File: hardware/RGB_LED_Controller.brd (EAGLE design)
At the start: 60 x 37 mm, 17 parts, among them IC2 MEGA8-AI, J2 CON_HEADER_1X04, Q1 MOSFET-NCHANNELFDD8580, Q2 MOSFET-NCHANNELFDD8580, Q4 MOSFET-NCHANNELFDD8580

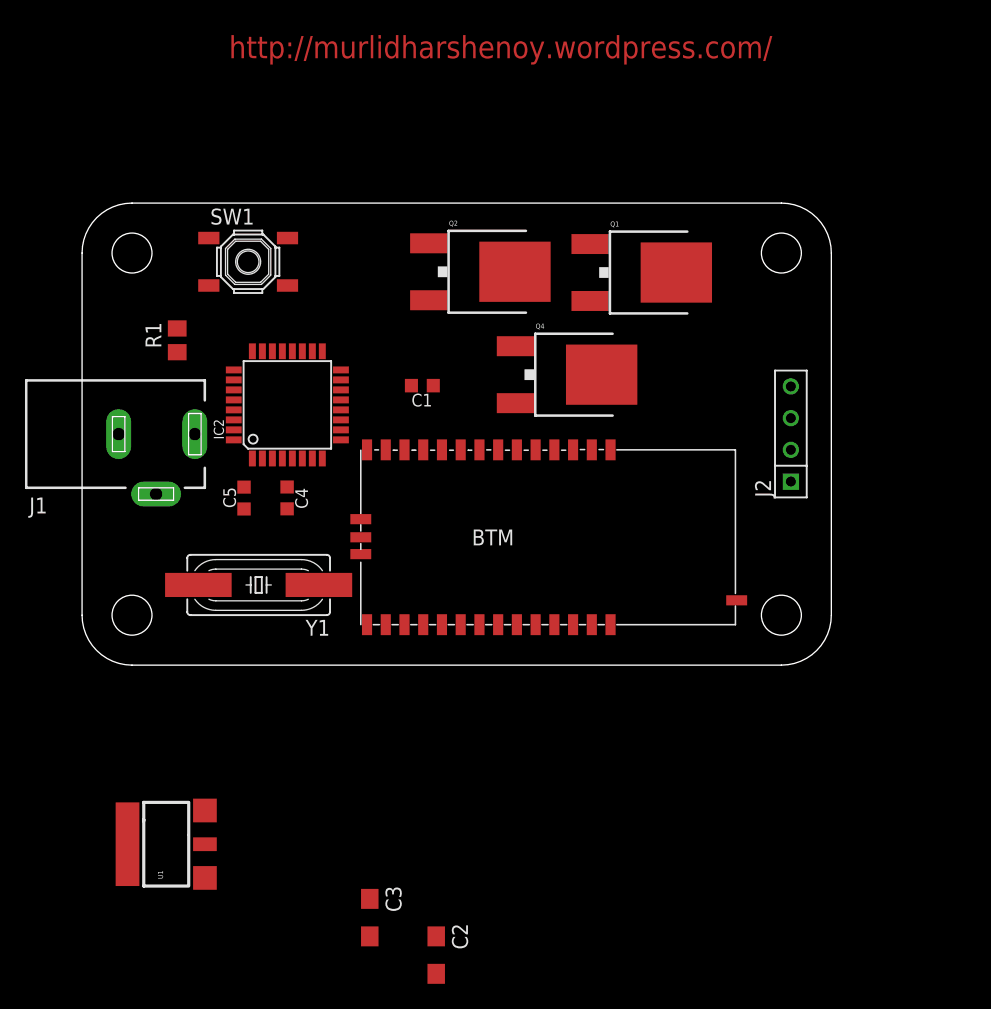
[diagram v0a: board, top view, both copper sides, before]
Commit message: some routing done. PCB modified to 7043
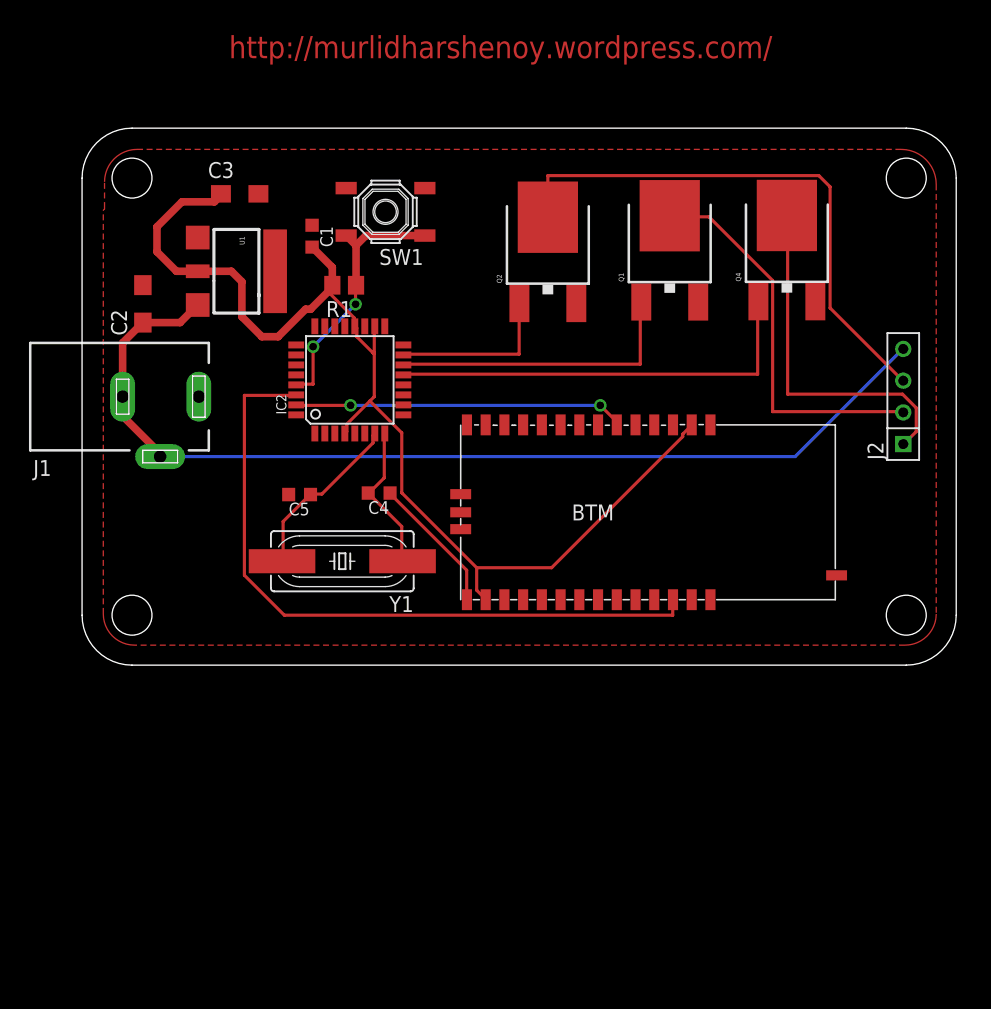
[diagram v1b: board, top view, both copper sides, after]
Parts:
- removed U$3: (no value), dp_devices:DP6037_V1
- added U$1: (no value), dp_devices:DP7043_V1
- moved C3 58.9 mm to (12.6, 37.7), turned to 0 degrees
- moved C2 57.2 mm to (4.87, 28.9), turned to 90 degrees
- moved U1 46.2 mm to (12.4, 31.5), turned to 270 degrees
- moved Q4 19.9 mm to (56.4, 34.4), turned to 0 degrees
- moved C1 14.9 mm to (18.4, 34.4), turned to 270 degrees
- moved R1 14.1 mm to (21.0, 30.4), turned to 180 degrees
- moved SW1 11.7 mm to (24.3, 36.3), turned to 180 degrees
- moved J2 9.49 mm to (65.8, 17.7)
- moved U$4 8.25 mm to (30.3, 5.24)
- moved C4 7.38 mm to (23.8, 13.8), turned to 180 degrees
- moved Y1 6.96 mm to (20.8, 8.32)
- moved IC2 5.39 mm to (21.4, 22.8)
- moved Q2 5.05 mm to (37.3, 34.3), turned to 0 degrees
- moved C5 4.46 mm to (17.4, 13.7), turned to 180 degrees
- moved Q1 3.14 mm to (47.1, 34.4), turned to 0 degrees
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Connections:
- net GND: now also U$4.PIO5
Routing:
- net +3V3: track 0.00 -> 91.0 mm
- net 12V: track 0.00 -> 80.8 mm
- net TX: track 0.00 -> 55.4 mm
- net N$8: track 0.00 -> 44.3 mm
- net N$1: track 0.00 -> 34.3 mm
- net N$7: track 0.00 -> 31.4 mm
- net N$6: track 0.00 -> 28.5 mm
- net RX: track 0.00 -> 26.5 mm, vias 0 -> 2
- net N$2: track 0.00 -> 24.0 mm
- net N$4: track 0.00 -> 20.9 mm, vias 0 -> 2
- net N$5: track 0.00 -> 13.8 mm
- net N$3: track 0.00 -> 13.4 mm
- net N$9: track 0.00 -> 11.9 mm
- net GND: track 0.00 -> 11.2 mm
- added copper zone on layer 1, net GND
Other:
- board size 60 x 37 mm -> 70 x 43 mm

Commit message: routing done.Optimize before printing
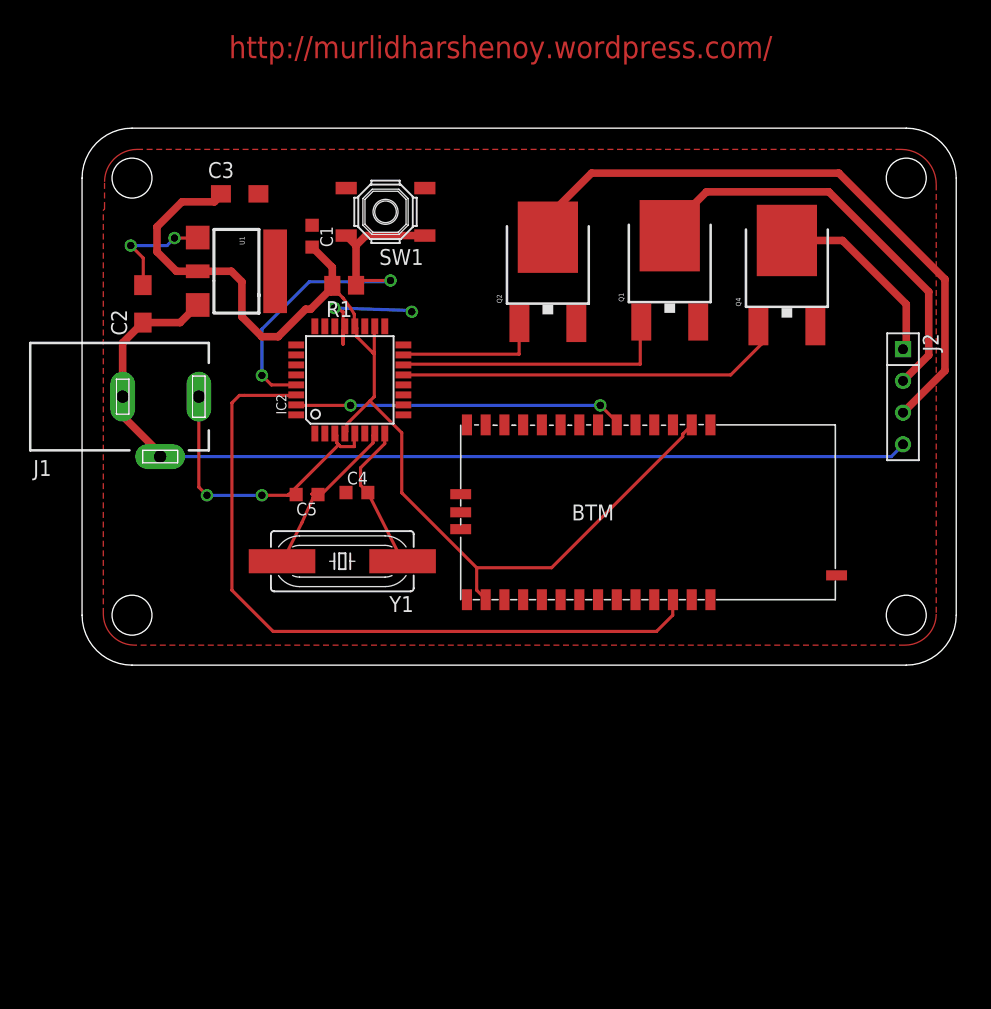
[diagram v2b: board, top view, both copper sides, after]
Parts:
- moved J2 7.60 mm to (65.7, 25.3), turned to 270 degrees
- moved Q4 2.00 mm to (56.4, 32.4)
- moved C4 1.78 mm to (22.0, 13.8), turned to 0 degrees
- moved Q1 1.60 mm to (47.1, 32.8)
- moved Q2 1.60 mm to (37.3, 32.7)
- moved C5 0.60 mm to (18.0, 13.7)
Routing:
- net GND: track 11.2 -> 46.6 mm, vias 0 -> 6
- net N$6: track 28.5 -> 15.4 mm
- net N$4: track 20.9 -> 31.7 mm
- net N$8: track 44.3 -> 50.5 mm
- net TX: track 55.4 -> 58.9 mm
- net 12V: track 80.8 -> 77.7 mm
- net N$1: track 34.3 -> 31.2 mm
- net N$7: track 31.4 -> 33.8 mm
- net N$2: track 24.0 -> 22.4 mm
- net N$3: track 13.4 -> 11.8 mm

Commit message: PCB labelled
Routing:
- net 12V: track 77.7 -> 82.4 mm
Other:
- board text added: "11.2012"
- board text added: "BT LED CNTRLR V2"
- board text added: "MURALIDHAR S."
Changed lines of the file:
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@@
 <?xml version="1.0" encoding="utf-8"?>
 <!DOCTYPE eagle SYSTEM "eagle.dtd">
-<eagle version="6.2">
+<eagle version="6.1">
 <drawing>
 <settings>
@@
 <board>
 <plain>
-<text x="11.76" y="48.6" size="1.778" layer="1">http://murlidharshenoy.wordpress.com/</text>
+<text x="7.66" y="40.7" size="1.778" layer="27">http://murlidharshenoy.wordpress.com/</text>
 <polygon width="0.4064" layer="41">
 <vertex x="52.2" y="19.4"/>
@@
 <vertex x="51.5" y="19.4"/>
 </polygon>
+<text x="62.1" y="26.7" size="1.778" layer="1" rot="R270">MURALIDHAR S.</text>
+<text x="8.6" y="39.3" size="1.27" layer="1">BT LED CNTRLR V2</text>
+<text x="66.9" y="18.2" size="1.778" layer="1" rot="R270">11.2012</text>
 </plain>
 <attributes>
@@
 <wire x1="6.3" y1="16.7" x2="6.4" y2="16.8" width="0.254" layer="1"/>
 <wire x1="6.3" y1="16.7" x2="6.25" y2="16.7" width="0.254" layer="1"/>
-<wire x1="64.8" y1="16.7" x2="65.7" y2="17.6" width="0.254" layer="16"/>
-<wire x1="6.3" y1="16.7" x2="64.8" y2="16.7" width="0.254" layer="16"/>
+<wire x1="64.7" y1="17.6" x2="65.7" y2="17.6" width="0.8128" layer="16"/>
 <wire x1="65.7" y1="17.6" x2="65.74" y2="17.68" width="0.254" layer="16"/>
 <wire x1="6.3" y1="16.7" x2="6.25" y2="16.7" width="0.254" layer="16"/>
+<wire x1="6.3" y1="16.7" x2="30.9" y2="16.7" width="0.8128" layer="16"/>
+<wire x1="30.9" y1="16.7" x2="30.9" y2="19.4" width="0.8128" layer="16"/>
+<wire x1="30.9" y1="19.4" x2="43.1" y2="19.4" width="0.8128" layer="16"/>
+<wire x1="43.1" y1="19.4" x2="43.1" y2="20.7" width="0.8128" layer="16"/>
+<wire x1="43.1" y1="20.7" x2="60.8" y2="20.7" width="0.8128" layer="16"/>
+<wire x1="60.8" y1="20.7" x2="64.7" y2="17.6" width="0.8128" layer="16"/>
 </signal>
 <signal name="N$4">

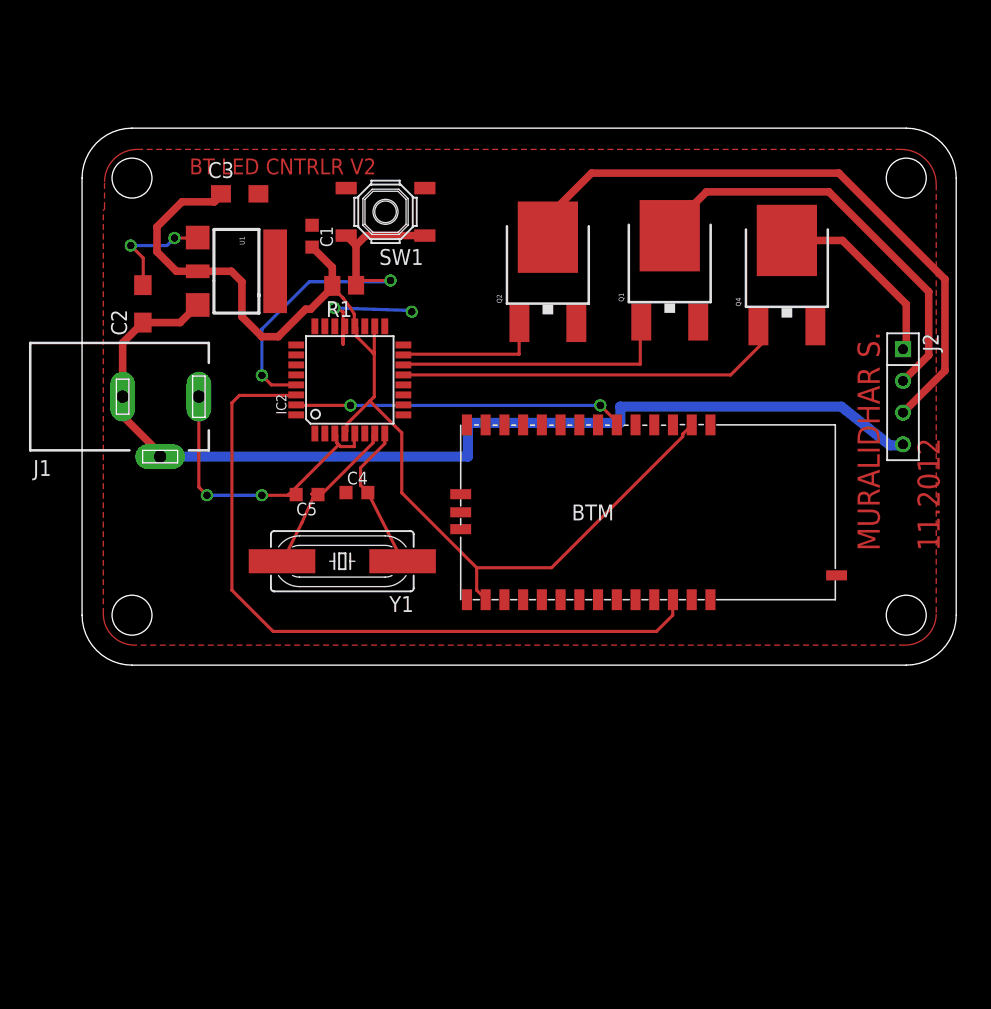
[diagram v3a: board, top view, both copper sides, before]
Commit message: OSHW logo added.Some track optimisations
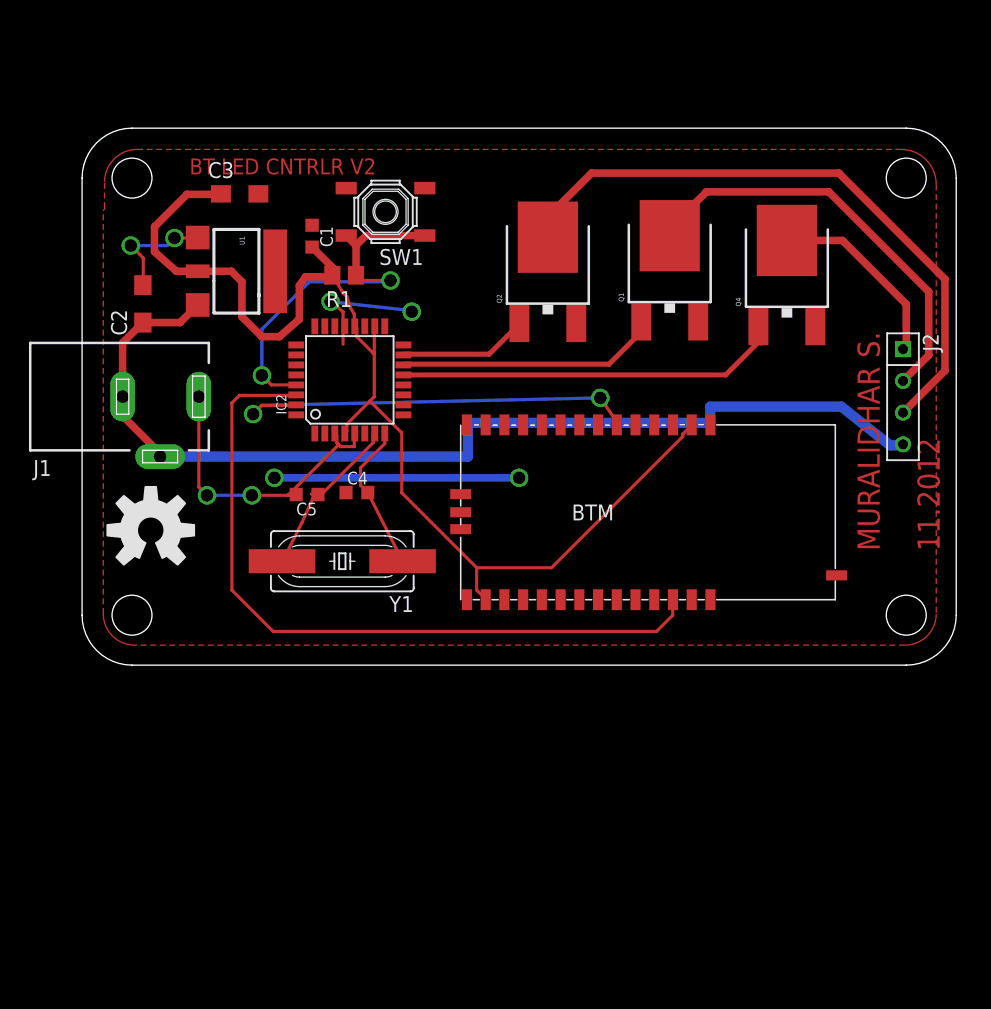
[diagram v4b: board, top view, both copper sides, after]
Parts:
- added E$1: (no value), SparkFun:OSHW-LOGO-L
- moved R1 0.80 mm to (21.0, 31.2)
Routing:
- net GND: track 46.6 -> 65.8 mm, vias 6 -> 8
- net RX: track 26.5 -> 34.5 mm
- net +3V3: track 91.5 -> 93.7 mm
- net N$2: track 22.4 -> 20.9 mm
- net N$3: track 11.8 -> 10.4 mm
- net N$1: track 31.2 -> 32.1 mm
- net N$4: track 31.7 -> 31.0 mm
